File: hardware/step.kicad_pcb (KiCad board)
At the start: 4 copper layers, 150 x 35 mm, 127 parts, among them J101 Conn_01x01, J102 Conn_01x01, J103 CORTEX-DEBUG, J1901 2x05_Horizontal, J2001 2x05_Horizontal, J201 Conn_01x01, J202 Conn_01x01, J203 Conn_01x01, J204 Conn_01x01, J301 Conn_01x01, J302 Conn_01x01, J303 Conn_01x01, J304 Conn_01x01, J401 Conn_01x01, J402 Conn_01x01, J403 Conn_01x01, J404 Conn_01x01, J501 Conn_01x01, J502 Conn_01x01, J503 Conn_01x01, J504 Conn_01x01, SW101 SW_Push, SW102 SW_Push, U101 ATSAMD51J, U102 TPS78433QWDRBRQ1, U1901 THVD24x2, U2001 THVD24x2, U201 TMC2130-LA, U301 TMC2130-LA, U401 TMC2130-LA, U501 TMC2130-LA, Y101 32k768

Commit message: Update parts library
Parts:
- C101, C102, C103, C104, C105, C106, C107, C108, C109, C1901, C2001, C201, C205, C206, C207, C208, C301, C305, C306, C307, C308, C401, C405, C406, C407, C408, C501, C505, C506, C507, C508: footprint Capacitor_SMD:C_0603_1608Metric -> V2_Capacitor_SMD:C_0603
- C110, C111: footprint Capacitor_SMD:C_0805_2012Metric -> V2_Capacitor_SMD:C_0603
- C202, C302, C402, C502: footprint Capacitor_SMD:CP_Elec_6.3x5.8 -> V2_Capacitor_SMD:CP_Elec_6.3x5.8
- C203, C204, C303, C304, C403, C404, C503, C504: footprint Capacitor_SMD:C_1210_3225Metric -> V2_Capacitor_SMD:C_1210
- D101: footprint LED_SMD:LED_0603_1608Metric -> V2_LED:LED_0603
- FID101, FID102, FID103: value Fiducial -> Fiducial_Paste
- INFO102: value ORDER-NUMBER -> Order_Number
- J101, J102, J201, J202, J203, J204, J301, J302, J303, J304, J401, J402, J403, J404, J501, J502, J503, J504: value Conn_01x01 -> WAGO 2065-100
- J103: value CORTEX-DEBUG -> Cortex_Debug
- R101, R102, R103, R104, R105, R1901, R2001, R201, R301, R401, R501: footprint Resistor_SMD:R_0603_1608Metric -> V2_Resistor_SMD:R_0603
- R202, R203, R302, R303, R402, R403, R502, R503: footprint Resistor_SMD:R_0805_2012Metric -> V2_Resistor_SMD:R_0805
- SW101, SW102: value SW_Push -> SKSG
- TVS101: value SMAJ36CA -> SMBJ36CA; footprint Diode_SMD:D_SMA -> V2_Diode_SMD:D_SMB
- TVS102: footprint Diode_SMD:D_0603_1608Metric -> V2_Diode_SMD:D_0603
- U1901, U2001: value THVD24x2 -> THVD2442

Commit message: Update parts
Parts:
- C110, C111: footprint V2_Capacitor_SMD:C_0603 -> V2_Capacitor_SMD:C_0805
- C206, C306, C406, C506: value 0u470 -> 0u47
- moved C110 0.25 mm to (79.5, 101.2)
- moved C111 0.25 mm to (79.5, 94.8)
- moved TVS102 0.25 mm to (79.5, 103.2)
- moved U102 0.25 mm to (79.5, 98.0)

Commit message: Refresh
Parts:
- TVS101: value SMBJ36CA -> SMBJ33CA
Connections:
- net +24V renamed +28V

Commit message: Update library
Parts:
- J103: value Cortex_Debug -> >VALUE; footprint V2_Cortex_Debug:Cortex_Debug_Pad -> V2_Connector_Debug:Cortex
- U201, U301, U401, U501: footprint V2_Driver_Stepper:QFN36-5X6 -> V2_Package_DFN_QFN:QFN36-5X6
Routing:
- net /SWCLK: track 11.7 -> 12.9 mm
- net GND: vias 146 -> 144
- net +3V3: vias 16 -> 15

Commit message: Use date as revision
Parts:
- J103: value >VALUE -> Cortex

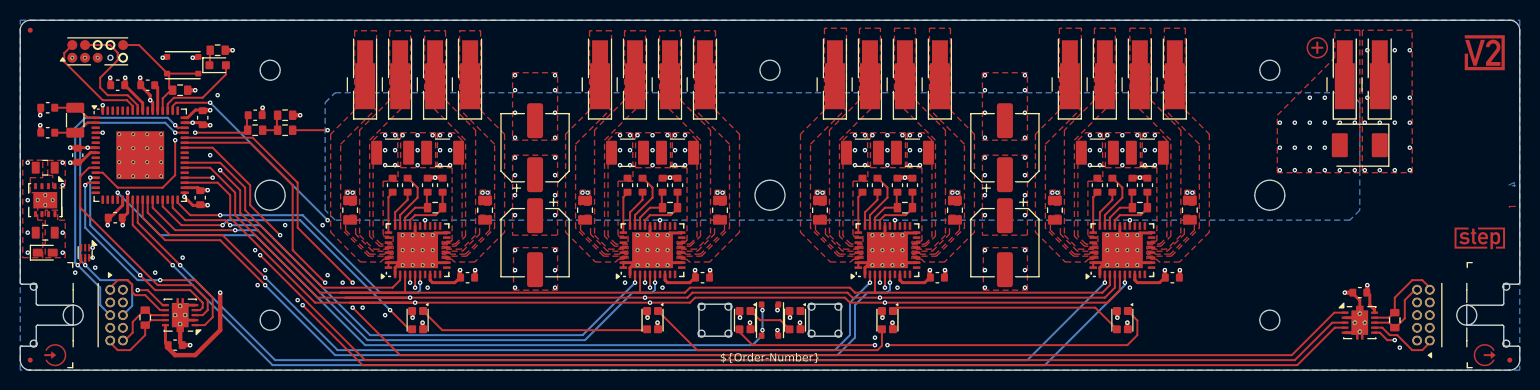
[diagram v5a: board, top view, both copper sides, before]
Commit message: Replace Order_Number
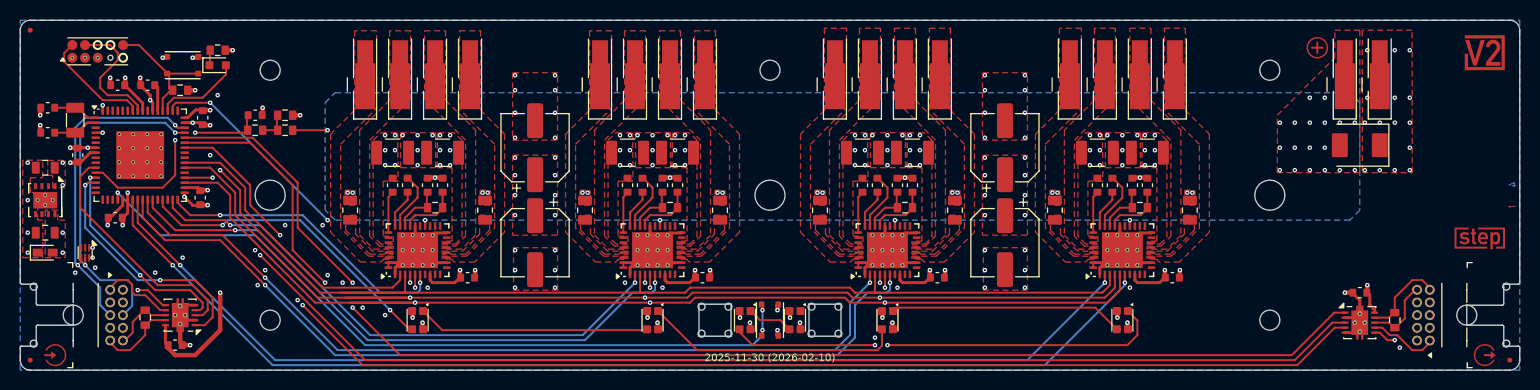
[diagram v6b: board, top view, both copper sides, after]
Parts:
- H101, H103, H105, H107, H108: value MountingHole_2mm -> 2mm
- H102, H104, H106: value MountingHole_3mm -> 3mm
- INFO102: value Order_Number -> ~; footprint V2_Production:Order_Number -> V2_Production:Revision
